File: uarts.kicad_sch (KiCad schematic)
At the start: 50 parts, among them J1 USB_C, U1 AT93C46D-TH-T, U5 FT4232HL, U8 74HC595D, Y1 12M

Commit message: Schematic V1 done
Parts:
- added D9: GRN, LED_SMD:LED_0603_1608Metric, symbol Device:LED
- added FB2: 600R/100M, Inductor_SMD:L_0805_2012Metric, symbol Device:FerriteBead_Small
- added R23: 330R, Resistor_SMD:R_0603_1608Metric, symbol Device:R_Small
- C10: renamed from C44; footprint (none) -> Capacitor_SMD:C_0603_1608Metric
- C11: renamed from C34; footprint (none) -> Capacitor_SMD:C_0603_1608Metric
- C12: renamed from C45; footprint (none) -> Capacitor_SMD:C_0603_1608Metric
- C13: renamed from C46; footprint (none) -> Capacitor_SMD:C_0603_1608Metric
- C14: renamed from C38; footprint (none) -> Capacitor_SMD:C_0603_1608Metric
- C15: renamed from C37; footprint (none) -> Capacitor_SMD:C_0603_1608Metric
- C16: renamed from C40; footprint (none) -> Capacitor_SMD:C_0603_1608Metric
- C17: renamed from C39; footprint (none) -> Capacitor_SMD:C_0603_1608Metric
- C18: renamed from C41; footprint (none) -> Capacitor_SMD:C_0603_1608Metric
- C19: renamed from C42; footprint (none) -> Capacitor_SMD:C_0603_1608Metric
- C20: renamed from C43; footprint (none) -> Capacitor_SMD:C_0603_1608Metric
- C3: renamed from C58; footprint (none) -> Capacitor_SMD:C_0603_1608Metric
- C4: renamed from C33; footprint (none) -> Capacitor_SMD:C_0603_1608Metric
- C5: renamed from C31; footprint (none) -> Capacitor_SMD:C_0603_1608Metric
- C6: renamed from C32; footprint (none) -> Capacitor_SMD:C_0603_1608Metric
- C7: renamed from C1; footprint (none) -> Capacitor_SMD:C_0603_1608Metric
- C8: renamed from C35; footprint (none) -> Capacitor_SMD:C_0603_1608Metric
- C9: renamed from C36; footprint (none) -> Capacitor_SMD:C_0603_1608Metric
- D1: renamed from D5; footprint (none) -> LED_SMD:LED_0603_1608Metric
- D2: renamed from D6; footprint (none) -> LED_SMD:LED_0603_1608Metric
- D3: renamed from D7; footprint (none) -> LED_SMD:LED_0603_1608Metric
- D4: renamed from D8; footprint (none) -> LED_SMD:LED_0603_1608Metric
- D5: renamed from D9; footprint (none) -> LED_SMD:LED_0603_1608Metric
- D6: renamed from D10; footprint (none) -> LED_SMD:LED_0603_1608Metric
- D7: renamed from D11; footprint (none) -> LED_SMD:LED_0603_1608Metric
- D8: renamed from D4; footprint (none) -> LED_SMD:LED_0603_1608Metric
- FB3: renamed from FB1; footprint (none) -> Inductor_SMD:L_0805_2012Metric; LCSC (none) -> C1017
- FB4: renamed from FB2; footprint (none) -> Inductor_SMD:L_0805_2012Metric; LCSC (none) -> C1017
- J1: footprint (none) -> Connector_USB:USB_C_Receptacle_GCT_USB4110; LCSC (none) -> C963217
- R10: renamed from R47; footprint (none) -> Resistor_SMD:R_0603_1608Metric
- R11: renamed from R48; footprint (none) -> Resistor_SMD:R_0603_1608Metric
- R12: renamed from R49; footprint (none) -> Resistor_SMD:R_0603_1608Metric
- R13: renamed from R50; footprint (none) -> Resistor_SMD:R_0603_1608Metric
- R14: renamed from R51; footprint (none) -> Resistor_SMD:R_0603_1608Metric
- R15: renamed from R52; footprint (none) -> Resistor_SMD:R_0603_1608Metric
- R16: renamed from R53; footprint (none) -> Resistor_SMD:R_0603_1608Metric
- R17: renamed from R1; footprint (none) -> Resistor_SMD:R_0603_1608Metric
- R18: renamed from R2; footprint (none) -> Resistor_SMD:R_0603_1608Metric
- R19: renamed from R35; footprint (none) -> Resistor_SMD:R_0603_1608Metric
- R20: renamed from R36; footprint (none) -> Resistor_SMD:R_0603_1608Metric
- R21: renamed from R37; footprint (none) -> Resistor_SMD:R_0603_1608Metric
- R22: renamed from R38; footprint (none) -> Resistor_SMD:R_0603_1608Metric
- R6: renamed from R43; footprint (none) -> Resistor_SMD:R_0603_1608Metric
- R7: renamed from R33; footprint (none) -> Resistor_SMD:R_0603_1608Metric
- R8: renamed from R34; footprint (none) -> Resistor_SMD:R_0603_1608Metric
- R9: renamed from R44; footprint (none) -> Resistor_SMD:R_0603_1608Metric
- Y1: footprint (none) -> Crystal:Crystal_SMD_3225-4Pin_3.2x2.5mm; LCSC (none) -> C362340
- renumbered U8 to U2, U1 to U3, U5 to U4
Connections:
- net +3V3: now also R23.1
- net +5V: now also FB2.1; no longer J1.A4 (VBUS), J1.A9 (VBUS), J1.B4 (VBUS), J1.B9 (VBUS)
- net FTDI_PWREN: no longer U4.60 (~{PWREN})
- new net: D9.1 (K), U4.60 (~{PWREN})
- new net: D9.2 (A), R23.2
- new net: FB2.2, J1.A4 (VBUS), J1.A9 (VBUS), J1.B4 (VBUS), J1.B9 (VBUS)
- no-connect marks 16 -> 17
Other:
- note added: "UART ACT LEDs"
- company: (none) -> M1GEO & G8OCV
- title: (none) -> Quad AMBE-3000R Board
- moved on the sheet: C11, C14, C3, C4, C7, D1, D2, D3, D4, D5, D6, D7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

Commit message: Most of the layout done
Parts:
- removed C10: 100n, Capacitor_SMD:C_0603_1608Metric, symbol Device:C_Small
- removed D9: GRN, LED_SMD:LED_0603_1608Metric, symbol Device:LED
- removed J1: USB_C, Connector_USB:USB_C_Receptacle_GCT_USB4110, symbol Connector:USB_C_Receptacle_USB2.0_14P
- removed R23: 330R, Resistor_SMD:R_0603_1608Metric, symbol Device:R_Small
- added J1: USB_C, Connector_USB:USB_C_Receptacle_GCT_USB4110, symbol Connector:USB_C_Receptacle_USB2.0_16P
- renumbered C11 to C10, C12 to C11, C13 to C12, C14 to C13, C15 to C14, C16 to C15, C17 to C16, C18 to C17, C19 to C18, C20 to C19
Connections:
- net FTDI_PWREN: now also U4.60 (~{PWREN})
- net GND: now also J1.A1 (GND), J1.A12 (GND), J1.B1 (GND), J1.B12 (GND), J1.S1 (SHIELD)
- net at R7.1: now also J1.A5 (CC1)
- net at FB2.2: now also J1.A4 (VBUS), J1.A9 (VBUS), J1.B4 (VBUS), J1.B9 (VBUS)
- net at C10.2, U4.2 (OSCI): now also Y1.3; no longer Y1.1
- net at C13.2, U4.3 (OSCO): now also Y1.1; no longer Y1.3
- net at R8.1: now also J1.B5 (CC2)
- net USB_Dm renamed USB_D-
- net USB_D-: now also J1.A7 (D-), J1.B7 (D-)
- net USB_Dp renamed USB_D+
- net USB_D+: now also J1.A6 (D+), J1.B6 (D+)
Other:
- note added: "1.8V VCORE"
- note removed: "1.8V VCORE Decoup."

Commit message: Final updates before manufacture of V1.00
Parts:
- C10, C13: value 27p -> 30p; LCSC (none) -> C1658
- C11, C12, C14, C16, C17, C18, C19, C3, C4, C5, C7, C9: LCSC (none) -> C14663
- C15, C6, C8: LCSC (none) -> C19666
- D1, D3, D5, D7: LCSC (none) -> C12624
- D2, D4, D6, D8: LCSC (none) -> C2286
- R10, R11, R12, R13, R14, R15, R16, R9: LCSC (none) -> C23138
- R17, R18, R20, R6: LCSC (none) -> C25804
- R19, R21: LCSC (none) -> C21190
- R22: LCSC (none) -> C22790
- R7, R8: LCSC (none) -> C23186
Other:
- title: Quad AMBE-3000R Board -> Quad AMBE-3000R Board (USB & UARTs)

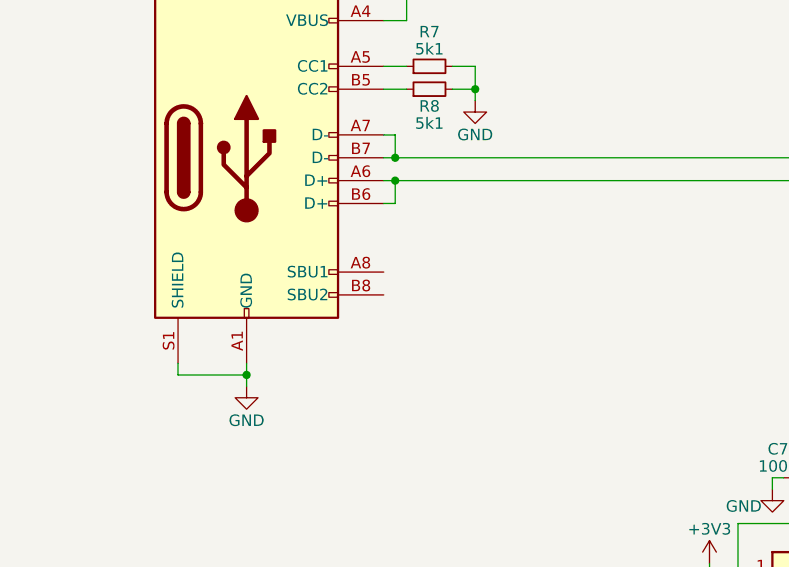
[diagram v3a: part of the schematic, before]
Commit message: Fixed USB C BoM option.
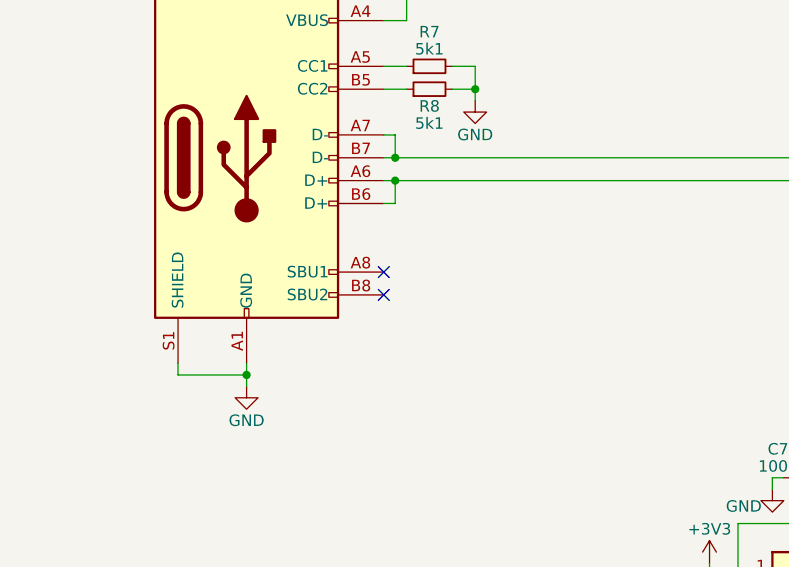
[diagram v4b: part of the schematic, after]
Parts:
- J1: LCSC C963217 -> C5187472
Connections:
- no-connect marks 17 -> 19
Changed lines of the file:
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@@
   (junction (at 134.62 142.24) (diameter 0) (color 0 0 0 0)
   )
+  (no_connect (at 57.15 93.98))
   (no_connect (at 218.44 104.14))
   (no_connect (at 218.44 81.28))
@@
   (no_connect (at 218.44 127))
   (no_connect (at 218.44 66.04))
+  (no_connect (at 57.15 91.44))
   (no_connect (at 218.44 88.9))
   (no_connect (at 218.44 111.76))
@@
       (effects (font (size 1.27 1.27)) hide)
     )
-    (property "Datasheet" "https://datasheet.lcsc.com/lcsc/2304140030_G-Switch-GT-USB-7047B_C963217.pdf" (at 45.72 78.74 0)
-      (effects (font (size 1.27 1.27)) hide)
-    )
-    (property "LCSC" "C963217" (at 41.91 78.74 0)
-      (effects (font (size 1.27 1.27)) hide)
-    )
+    (property "Datasheet" "https://datasheet.lcsc.com/lcsc/2209291730_SHOU-HAN-TYPE-C-16P-QTWT_C5187472.pdf" (at 45.72 78.74 0)
+      (effects (font (size 1.27 1.27)) hide)
+    )
+    (property "LCSC" "C5187472" (at 41.91 78.74 0)
+      (effects (font (size 1.27 1.27)) hide)
+    )

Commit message: Changed Y1 part information from 24MHz to 12MHz
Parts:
- Y1: LCSC C362340 -> C362368
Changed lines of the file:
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@@
       (effects (font (size 1.27 1.27)) hide)
     )
-    (pin "2")
-    (pin "1")
+    (pin "1")
+    (pin "2")
     (instances
       (project "Quad-AMBE3000"
@@
       (effects (font (size 1.27 1.27)) hide)
     )
-    (pin "2")
-    (pin "1")
+    (pin "1")
+    (pin "2")
     (instances
       (project "Quad-AMBE3000"
@@
       (effects (font (size 1.27 1.27)) hide)
     )
+    (pin "A1")
+    (pin "A12")
+    (pin "A4")
+    (pin "A5")
     (pin "A6")
-    (pin "A4")
-    (pin "B7")
-    (pin "S1")
-    (pin "B6")
-    (pin "A9")
-    (pin "A1")
-    (pin "B8")
-    (pin "A12")
-    (pin "B9")
-    (pin "B5")
-    (pin "A5")
-    (pin "B4")
     (pin "A7")
     (pin "A8")
+    (pin "A9")
+    (pin "B1")
     (pin "B12")
-    (pin "B1")
+    (pin "B4")
+    (pin "B5")
+    (pin "B6")
+    (pin "B7")
+    (pin "B8")
+    (pin "B9")
+    (pin "S1")
     (instances
       (project "Quad-AMBE3000"
@@
       (effects (font (size 1.27 1.27)) hide)
     )
-    (pin "2")
-    (pin "1")
+    (pin "1")
+    (pin "2")
     (instances
       (project "Quad-AMBE3000"
@@
       (effects (font (size 1.27 1.27)) hide)
     )
-    (pin "2")
-    (pin "1")
+    (pin "1")
+    (pin "2")
     (instances
       (project "Quad-AMBE3000"
@@
       (effects (font (size 1.27 1.27)) hide)
     )
-    (pin "2")
-    (pin "1")
+    (pin "1")
+    (pin "2")
     (instances
       (project "Quad-AMBE3000"
@@
       (effects (font (size 1.27 1.27)) hide)
     )
-    (pin "2")
-    (pin "1")
+    (pin "1")
+    (pin "2")
     (instances
       (project "Quad-AMBE3000"
@@
       (effects (font (size 1.27 1.27)) hide)
     )
+    (pin "1")
+    (pin "10")
+    (pin "11")
+    (pin "12")
+    (pin "13")
+    (pin "14")
+    (pin "15")
+    (pin "16")
+    (pin "2")
+    (pin "3")
+    (pin "4")
     (pin "5")
-    (pin "13")
-    (pin "16")
-    (pin "2")
-    (pin "4")
+    (pin "6")
+    (pin "7")
     (pin "8")
     (pin "9")
-    (pin "6")
-    (pin "3")
-    (pin "10")
-    (pin "14")
-    (pin "11")
-    (pin "12")
-    (pin "7")
-    (pin "1")
-    (pin "15")
     (instances
       (project "Quad-AMBE3000"
@@
       (effects (font (size 1.27 1.27)) hide)
     )
-    (pin "2")
-    (pin "1")
+    (pin "1")
+    (pin "2")
     (instances
       (project "Quad-AMBE3000"
@@
       (effects (font (size 1.27 1.27)) hide)
     )
-    (pin "2")
-    (pin "1")
+    (pin "1")
+    (pin "2")
     (instances
       (project "Quad-AMBE3000"
@@
       (effects (font (size 1.27 1.27)) hide)
     )
-    (pin "2")
-    (pin "1")
+    (pin "1")
+    (pin "2")
     (instances
       (project "Quad-AMBE3000"
@@
       (effects (font (size 1.27 1.27)) hide)
     )
-    (property "Datasheet" "https://datasheet.lcsc.com/lcsc/1912111437_Yajingxin-TXM24M0004322FBCDO00T_C362340.pdf" (at 140.97 142.24 0)
-      (effects (font (size 1.27 1.27)) hide)
-    )
-    (property "LCSC" "C362340" (at 140.97 142.24 0)
-      (effects (font (size 1.27 1.27)) hide)
-    )
-    (pin "2")
+    (property "Datasheet" "https://datasheet.lcsc.com/lcsc/1912111437_Yajingxin-TXM12M0004322CBCDO00T_C362368.pdf" (at 140.97 142.24 0)
+      (effects (font (size 1.27 1.27)) hide)
+    )
+    (property "LCSC" "C362368" (at 140.97 142.24 0)
+      (effects (font (size 1.27 1.27)) hide)
+    )
+    (pin "1")
+    (pin "2")
+    (pin "3")
     (pin "4")
-    (pin "3")
-    (pin "1")
     (instances
       (project "Quad-AMBE3000"
@@
       (effects (font (size 1.27 1.27)) hide)
     )
-    (pin "2")
-    (pin "1")
+    (pin "1")
+    (pin "2")
     (instances
       (project "Quad-AMBE3000"
@@
       (effects (font (size 1.27 1.27)) hide)
     )
+    (pin "1")
+    (pin "10")
+    (pin "11")
+    (pin "12")
+    (pin "13")
+    (pin "14")
+    (pin "15")
+    (pin "16")
+    (pin "17")
+    (pin "18")
+    (pin "19")
+    (pin "2")
+    (pin "20")
+    (pin "21")
+    (pin "22")
+    (pin "23")
+    (pin "24")
+    (pin "25")
+    (pin "26")
+    (pin "27")
+    (pin "28")
     (pin "29")
-    (pin "56")
-    (pin "55")
+    (pin "3")
+    (pin "30")
+    (pin "31")
+    (pin "32")
+    (pin "33")
+    (pin "34")
+    (pin "35")
+    (pin "36")
+    (pin "37")
+    (pin "38")
+    (pin "39")
+    (pin "4")
+    (pin "40")
+    (pin "41")
+    (pin "42")
+    (pin "43")
+    (pin "44")
+    (pin "45")
+    (pin "46")
+    (pin "47")
+    (pin "48")
+    (pin "49")
+    (pin "5")
+    (pin "50")
+    (pin "51")
+    (pin "52")
     (pin "53")
     (pin "54")
+    (pin "55")
+    (pin "56")
+    (pin "57")
+    (pin "58")
+    (pin "59")
+    (pin "6")
+    (pin "60")
     (pin "61")
     (pin "62")
-    (pin "58")
-    (pin "15")
-    (pin "3")
-    (pin "52")
-    (pin "4")
-    (pin "51")
-    (pin "45")
-    (pin "59")
-    (pin "42")
-    (pin "21")
+    (pin "63")
     (pin "64")
-    (pin "16")
-    (pin "63")
-    (pin "18")
-    (pin "2")
+    (pin "7")
     (pin "8")
-    (pin "24")
-    (pin "20")
-    (pin "22")
-    (pin "43")
-    (pin "38")
-    (pin "47")
-    (pin "49")
-    (pin "50")
-    (pin "48")
-    (pin "36")
-    (pin "17")
-    (pin "28")
-    (pin "39")
-    (pin "31")
-    (pin "10")
-    (pin "60")
-    (pin "41")
-    (pin "11")
-    (pin "40")
-    (pin "30")
-    (pin "32")
-    (pin "5")
-    (pin "19")
-    (pin "57")
-    (pin "46")
     (pin "9")
-    (pin "13")
-    (pin "6")
-    (pin "44")
-    (pin "37")
-    (pin "23")
-    (pin "25")
-    (pin "34")
-    (pin "27")
-    (pin "14")
-    (pin "26")
-    (pin "7")
-    (pin "12")
-    (pin "33")
-    (pin "35")
-    (pin "1")
     (instances
       (project "Quad-AMBE3000"
@@
       (effects (font (size 1.27 1.27)) hide)
     )
-    (pin "2")
-    (pin "1")
+    (pin "1")
+    (pin "2")
     (instances
       (project "Quad-AMBE3000"
@@
       (effects (font (size 1.27 1.27)) hide)
     )
-    (pin "2")
-    (pin "1")
+    (pin "1")
+    (pin "2")
     (instances
       (project "Quad-AMBE3000"
@@
       (effects (font (size 1.27 1.27)) hide)
     )
-    (pin "2")
-    (pin "1")
+    (pin "1")
+    (pin "2")
     (instances
       (project "Quad-AMBE3000"
@@
       (effects (font (size 1.27 1.27)) hide)
     )
-    (pin "2")
-    (pin "1")
+    (pin "1")
+    (pin "2")
     (instances
       (project "Quad-AMBE3000"
@@
       (effects (font (size 1.27 1.27)) hide)
     )
-    (pin "2")
-    (pin "1")
+    (pin "1")
+    (pin "2")
     (instances
       (project "Quad-AMBE3000"
@@
       (effects (font (size 1.27 1.27)) hide)
     )
+    (pin "1")
+    (pin "2")
+    (pin "3")
+    (pin "4")
+    (pin "5")
+    (pin "6")
+    (pin "7")
     (pin "8")
-    (pin "6")
-    (pin "5")
-    (pin "4")
-    (pin "2")
-    (pin "3")
-    (pin "7")
-    (pin "1")
     (instances
       (project "Quad-AMBE3000"
@@
       (effects (font (size 1.27 1.27)) hide)
     )
-    (pin "2")
-    (pin "1")
+    (pin "1")
+    (pin "2")
     (instances
       (project "Quad-AMBE3000"
@@
       (effects (font (size 1.27 1.27)) hide)
     )
-    (pin "2")
-    (pin "1")
+    (pin "1")
+    (pin "2")
     (instances
       (project "Quad-AMBE3000"
@@
       (effects (font (size 1.27 1.27)) hide)
     )
-    (pin "2")
-    (pin "1")
+    (pin "1")
+    (pin "2")
     (instances
       (project "Quad-AMBE3000"
@@
       (effects (font (size 1.27 1.27)) hide)
     )
-    (pin "2")
-    (pin "1")
+    (pin "1")
+    (pin "2")
     (instances
       (project "Quad-AMBE3000"
@@
       (effects (font (size 1.27 1.27)) hide)
     )
-    (pin "2")
-    (pin "1")
-    (instances
-      (project "Quad-AMBE3000"
+    (pin "1")
+    (pin "2")
+    (instances
+      (project "Quad-AMBE3000"
